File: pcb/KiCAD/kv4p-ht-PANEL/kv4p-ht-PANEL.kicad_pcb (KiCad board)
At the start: 4 copper layers, 81.2 x 96.6 mm, 178 parts, among them J1 Antenna, J2 SMA, J4 SAO v.69bis, J5 USB-C Socket, J6 GPIO Header, Q1 SS8050, Q2 SS8050, Q3 AO3400A, SW1 PTT, SW2 PTT, SW3 Reset, SW4 Program, U1 DRA/SA818, U2 AZ1117H-3.3TRG1, U4 CP2102N-A02-GQFN24, U5 ESP32-WROOM-32E-N4

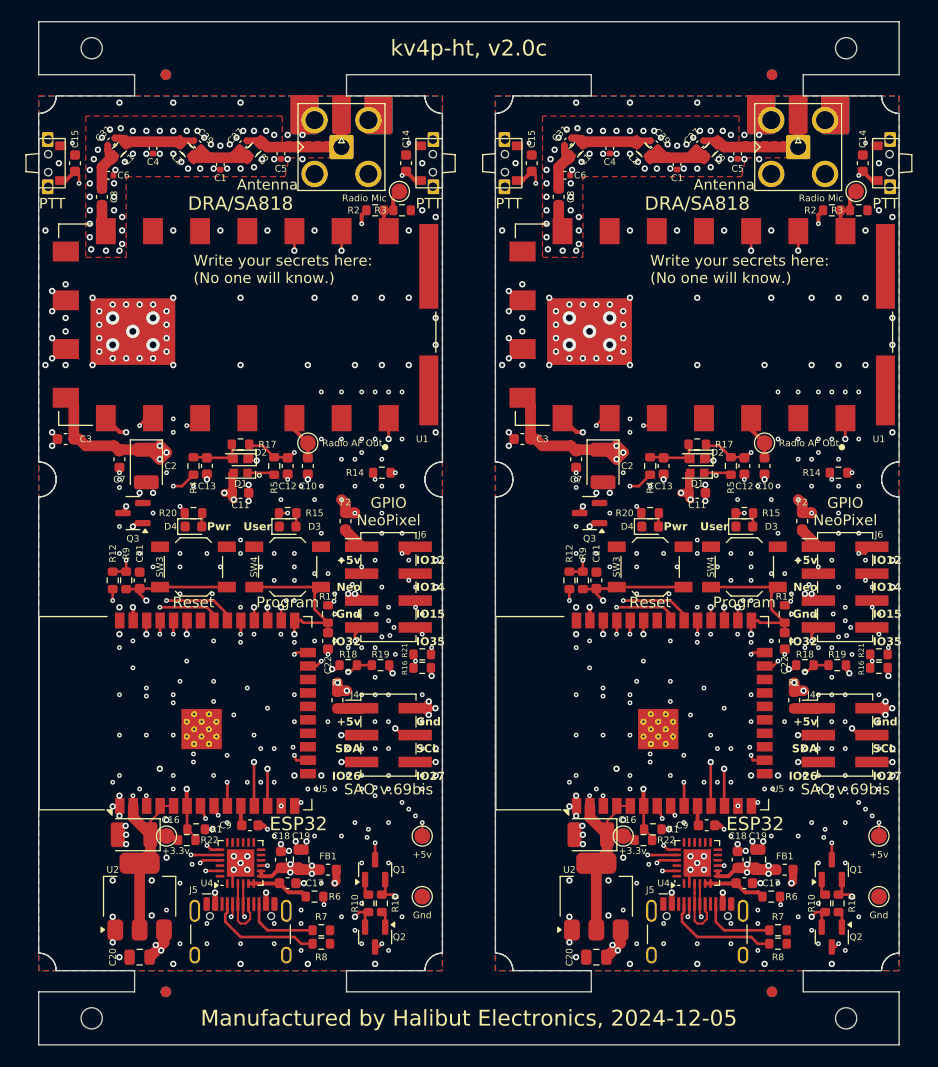
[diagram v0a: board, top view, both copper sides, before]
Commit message: Moved panel to its own project directory. #130
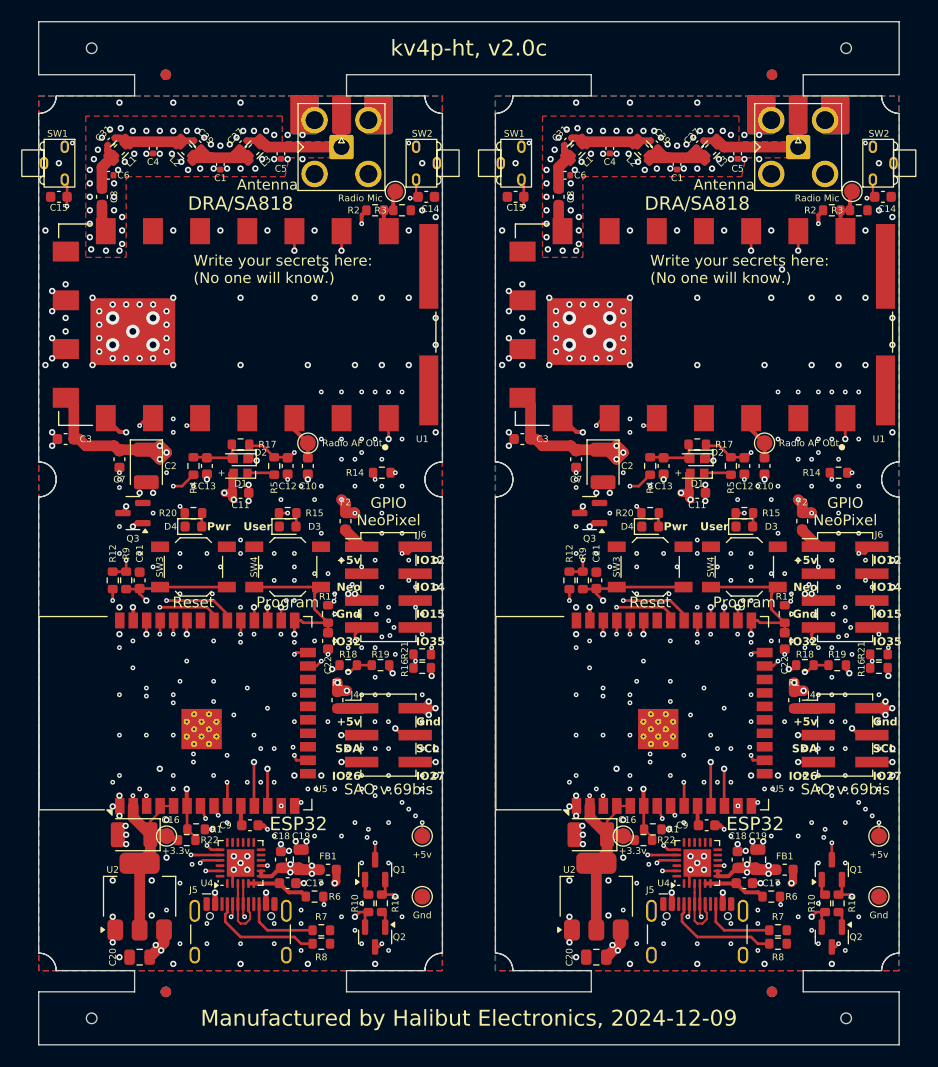
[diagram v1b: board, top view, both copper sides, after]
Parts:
- removed the C14 at (142.6, 33.4)
- removed the C14 at (185.7, 33.4)
- removed the C15 at (154.4, 33.4)
- removed the C15 at (111.3, 33.4)
- removed the L1 at (158.6, 32.1)
- removed the L1 at (115.5, 32.1)
- removed the L2 at (165.0, 32.1)
- removed the L2 at (121.9, 32.1)
- removed the L3 at (171.3, 32.1)
- removed the L3 at (128.2, 32.1)
- removed the L4 at (128.2, 32.1)
- removed the L4 at (171.3, 32.1)
- removed the SW1 at (107.9, 33.4)
- removed the SW1 at (151.0, 33.4)
- removed the SW2 at (146.0, 33.4)
- removed the SW2 at (189.1, 33.4)
- removed the TP4 at (185.0, 36.0)
- removed the TP4 at (141.9, 36.0)
- added C14: 2.2nF Tuned VHF, Capacitor_SMD:C_0603_1608Metric, F.Cu at (187.6, 36.5)
- added C14: 2.2nF Tuned VHF, Capacitor_SMD:C_0603_1608Metric, F.Cu at (144.5, 36.5)
- added C15: 2.2nF Tuned VHF, Capacitor_SMD:C_0603_1608Metric, F.Cu at (152.9, 36.5)
- added C15: 2.2nF Tuned VHF, Capacitor_SMD:C_0603_1608Metric, F.Cu at (109.8, 36.5)
- added L1: 27nH, Libraries:L_0805_2115Metric (Murata Inductors), F.Cu at (158.6, 32.1)
- added L1: 27nH, Libraries:L_0805_2115Metric (Murata Inductors), F.Cu at (115.5, 32.1)
- added L2: 30nH, Libraries:L_0805_2115Metric (Murata Inductors), F.Cu at (121.9, 32.1)
- added L2: 30nH, Libraries:L_0805_2115Metric (Murata Inductors), F.Cu at (165.0, 32.1)
- added L3: 43nH, Libraries:L_0805_2115Metric (Murata Inductors), F.Cu at (171.3, 32.1)
- added L3: 43nH, Libraries:L_0805_2115Metric (Murata Inductors), F.Cu at (128.2, 32.1)
- added L4: ~, Inductor_SMD:L_0603_1608Metric, F.Cu at (128.2, 32.1)
- added L4: ~, Inductor_SMD:L_0603_1608Metric, F.Cu at (171.3, 32.1)
- added SW1: PTT, kv4p-ht:SW-Push-SPST-Horizontal-C455252, F.Cu at (151.1, 33.4)
- added SW1: PTT, kv4p-ht:SW-Push-SPST-Horizontal-C455252, F.Cu at (108.0, 33.4)
- added SW2: PTT, kv4p-ht:SW-Push-SPST-Horizontal-C455252, F.Cu at (189.0, 33.4)
- added SW2: PTT, kv4p-ht:SW-Push-SPST-Horizontal-C455252, F.Cu at (145.9, 33.4)
- added TP4: Radio Mic, TestPoint:TestPoint_Pad_D1.5mm, F.Cu at (141.6, 36.0)
- added TP4: Radio Mic, TestPoint:TestPoint_Pad_D1.5mm, F.Cu at (184.7, 36.0)
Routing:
- net Board_1-/PTT Button Left: track 75.1 -> 72.9 mm
- net Board_0-/PTT Button Left: track 75.1 -> 72.9 mm
- net Board_0-/PTT Button Right: track 61.7 -> 60.1 mm
- net Board_1-/PTT Button Right: track 61.7 -> 60.1 mm
- net Board_1-/Radio Mic In: track 5.09 -> 4.28 mm
- net Board_0-/Radio Mic In: track 5.09 -> 4.28 mm
- net Board_1-GND: vias 185 -> 186
- net Board_0-GND: vias 185 -> 186
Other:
- board text added: "+"
- board text added: "Manufactured by Halibut Electronics, 2024-12-09"
- board text added: "kv4p HT, v2.0c 2024-12-09 VanceVagell v2 hardware by @SmittyHalibut"
- board text removed: "Manufactured by Halibut Electronics, 2024-12-05"
- board text removed: "kv4p HT, v2.0c 2024-12-05 VanceVagell v2 hardware by @SmittyHalibut"

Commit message: Moved the 2115 inductor outline into the shared library. #130
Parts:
- removed the L1 at (158.6, 32.1)
- removed the L1 at (115.5, 32.1)
- removed the L2 at (121.9, 32.1)
- removed the L2 at (165.0, 32.1)
- removed the L3 at (171.3, 32.1)
- removed the L3 at (128.2, 32.1)
- added L1: 27nH, kv4p-ht:L_0805_2115Metric (Murata Inductors), F.Cu at (115.5, 32.1)
- added L1: 27nH, kv4p-ht:L_0805_2115Metric (Murata Inductors), F.Cu at (158.6, 32.1)
- added L2: 30nH, kv4p-ht:L_0805_2115Metric (Murata Inductors), F.Cu at (121.9, 32.1)
- added L2: 30nH, kv4p-ht:L_0805_2115Metric (Murata Inductors), F.Cu at (165.0, 32.1)
- added L3: 43nH, kv4p-ht:L_0805_2115Metric (Murata Inductors), F.Cu at (171.3, 32.1)
- added L3: 43nH, kv4p-ht:L_0805_2115Metric (Murata Inductors), F.Cu at (128.2, 32.1)
